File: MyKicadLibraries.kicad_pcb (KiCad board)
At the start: 2 copper layers, 184.4 x 134.7 mm, 37 parts, among them J1 Conn_01x08, J10 RCJ-22, J11 DIN-5, J12 Mini-DIN-6, J13 USB_A, J14 Conn_01x02, J15 Conn_01x02, J2 Conn_01x08, J3 POGO Pins, J4 c8-inlet, J5 FTDI, J6 Micro_SD_Card, J7 Conn_01x04, J8 Conn_02x04_Counter_Clockwise, J9 Conn_01x04, SW1 Schurter Switch, U1 radio-receiver, U10 rdm-6300, U11 magnetic-charger, U12 adafruit-MAX98357, U13 TTL, U14 lxb18, U15 esp32-wemos-d1-mini, U16 TCRT5000, U17 opb607a, U18 max98367, U19 esp-01f, U2 tp4056, U3 LilygoSIMT7000G, U4 esp-01m, U5 relais_module, U6 ESP-01, U7 dcdc, U8 mems-mic, U9 ESP-12E

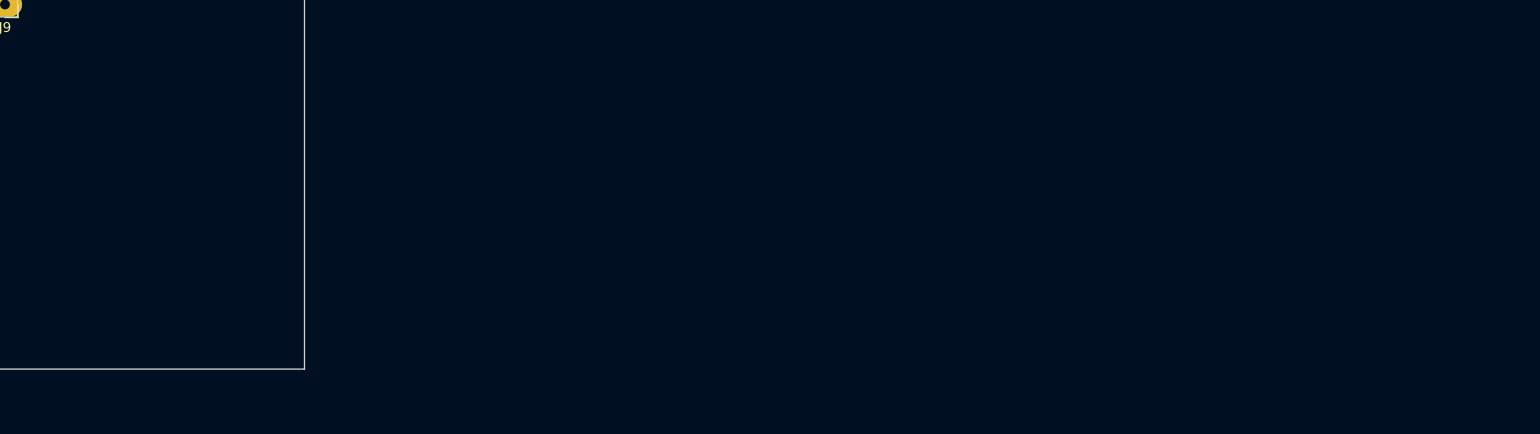
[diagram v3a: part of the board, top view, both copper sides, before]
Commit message: Add m18 bluetooth module
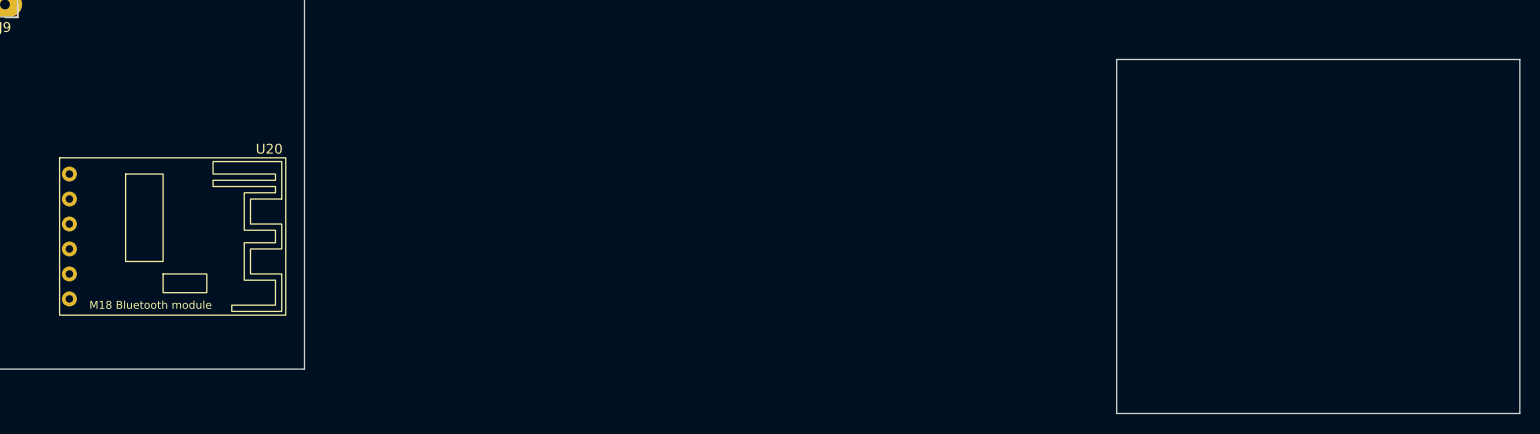
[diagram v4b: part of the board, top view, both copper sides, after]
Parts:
- added U20: m18, m18:m18, F.Cu at (228.5, 154.0)
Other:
- board size 184.4 x 134.7 mm -> 308 x 139.2 mm
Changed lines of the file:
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@@
   (net 264 "unconnected-(U19-Pad19)")
   (net 265 "unconnected-(U2-Pad6)")
+  (net 266 "unconnected-(U20-Pad1)")
+  (net 267 "unconnected-(U20-Pad2)")
+  (net 268 "unconnected-(U20-Pad3)")
+  (net 269 "unconnected-(U20-Pad4)")
+  (net 270 "unconnected-(U20-Pad5)")
+  (net 271 "unconnected-(U20-Pad6)")
   (footprint "esp-01f:esp-01f" (layer "F.Cu")
     (at 114.405 137.985)
@@
     )
   )
+  (footprint "m18:m18" (layer "F.Cu")
+    (at 228.5 154)
+    (property "Sheetfile" "MyKicadLibraries.kicad_sch")
+    (property "Sheetname" "")
+    (attr through_hole)
+    (fp_text reference "U20" (at 20.32 -8.89 unlocked) (layer "F.SilkS")
+      (effects (font (size 1 1) (thickness 0.15)))
+    )
+    (fp_text value "m18" (at 0 -8.89 unlocked) (layer "F.Fab")
+      (effects (font (size 1 1) (thickness 0.15)))
+    )
+    (fp_text user "M18 Bluetooth module" (at 8.255 6.985 unlocked) (layer "F.SilkS")
+      (effects (font (size 0.8 0.8) (thickness 0.15)))
+    )
+    (fp_text user "${REFERENCE}" (at 20.32 -8.89 unlocked) (layer "F.Fab")
+      (effects (font (size 1 1) (thickness 0.15)))
+    )
+    (fp_rect (start 5.715 -6.35) (end 9.525 2.54) (layer "F.SilkS") (width 0.12) (fill none))
+    (fp_rect (start 9.525 3.81) (end 13.97 5.715) (layer "F.SilkS") (width 0.12) (fill none))
+    (fp_rect (start -1 -8) (end 22 8) (layer "F.SilkS") (width 0.12) (fill none))
+    (fp_poly (pts
+        (xy 21.59 -3.81)
+        (xy 18.415 -3.81)
+        (xy 18.415 -1.27)
+        (xy 21.59 -1.27)
+        (xy 21.59 1.27)
+        (xy 18.415 1.27)
+        (xy 18.415 3.81)
+        (xy 21.59 3.81)
+        (xy 21.59 7.62)
+        (xy 16.51 7.62)
+        (xy 16.51 6.985)
+        (xy 20.955 6.985)
+        (xy 20.955 4.445)
+        (xy 17.78 4.445)
+        (xy 17.78 0.635)
+        (xy 20.955 0.635)
+        (xy 20.955 -0.635)
+        (xy 17.78 -0.635)
+        (xy 17.78 -4.445)
+        (xy 20.955 -4.445)
+        (xy 20.955 -5.08)
+        (xy 14.605 -5.08)
+        (xy 14.605 -5.715)
+        (xy 20.955 -5.715)
+        (xy 20.955 -6.35)
+        (xy 14.605 -6.35)
+        (xy 14.605 -7.62)
+        (xy 21.59 -7.62)
+      ) (layer "F.SilkS") (width 0.12) (fill none))
+    (pad "1" thru_hole circle (at 0 -6.35) (size 1.524 1.524) (drill 0.762) (layers *.Cu *.Mask)
+      (net 266 "unconnected-(U20-Pad1)") (pinfunction "R") (pintype "input"))
+    (pad "2" thru_hole circle (at 0 -3.81) (size 1.524 1.524) (drill 0.762) (layers *.Cu *.Mask)
+      (net 267 "unconnected-(U20-Pad2)") (pinfunction "L") (pintype "input"))
+    (pad "3" thru_hole circle (at 0 -1.27) (size 1.524 1.524) (drill 0.762) (layers *.Cu *.Mask)
+      (net 268 "unconnected-(U20-Pad3)") (pinfunction "GND") (pintype "power_in"))
+    (pad "4" thru_hole circle (at 0 1.27) (size 1.524 1.524) (drill 0.762) (layers *.Cu *.Mask)
+      (net 269 "unconnected-(U20-Pad4)") (pinfunction "VCC") (pintype "power_in"))
+    (pad "5" thru_hole circle (at 0 3.81) (size 1.524 1.524) (drill 0.762) (layers *.Cu *.Mask)
+      (net 270 "unconnected-(U20-Pad5)") (pinfunction "MUTE") (pintype "input"))
+    (pad "6" thru_hole circle (at 0 6.35) (size 1.524 1.524) (drill 0.762) (layers *.Cu *.Mask)
+      (net 271 "unconnected-(U20-Pad6)") (pinfunction "KEY") (pintype "input"))
+    (model "${KIPRJMOD}/lib/m18/m18.step"
+      (offset (xyz 13.9 -16.3 -9.3))
+      (scale (xyz 1 1 1))
+      (rotate (xyz -90 0 -180))
+    )
+  )
   (footprint "neopixel-strip:neopixel-strip" (layer "F.Cu")
     (at 72.593 100.941 90)
@@
   (gr_rect (start 206.705 143.105) (end 219.405 150.725) (layer "Edge.Cuts") (width 0.1) (fill none))
   (gr_rect (start 68.042948 32.770045) (end 252.405 167.485) (layer "Edge.Cuts") (width 0.1) (fill none))
+  (gr_rect (start 335 136) (end 376 172) (layer "Edge.Cuts") (width 0.1) (fill none))
   (segment (start 72.593 104.497) (end 90.881 104.497) (width 0.8) (layer "F.Cu") (net 82))
   (segment (start 72.593 97.385) (end 90.881 97.385) (width 0.8) (layer "F.Cu") (net 83))

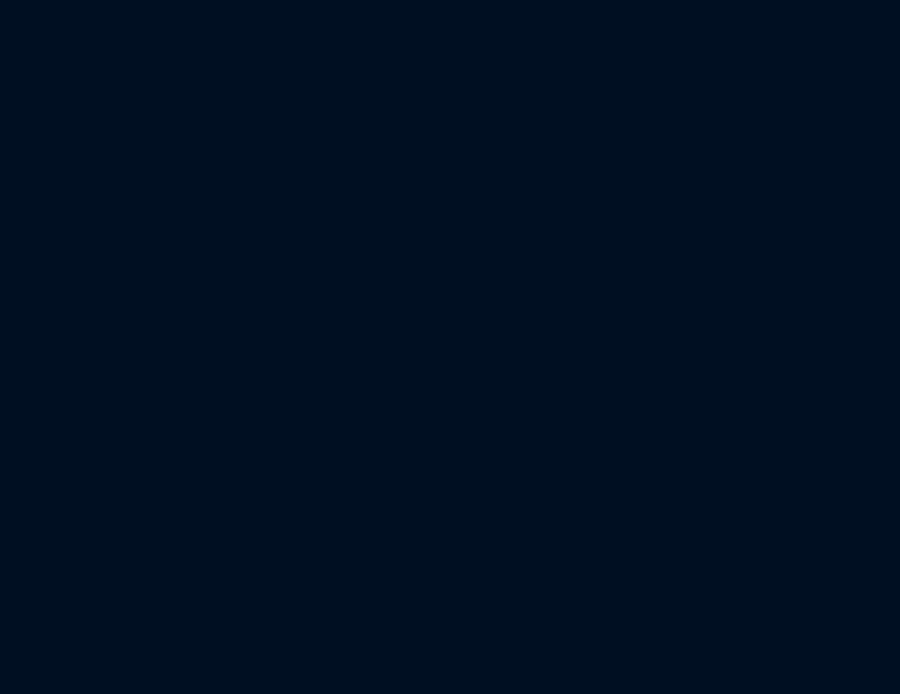
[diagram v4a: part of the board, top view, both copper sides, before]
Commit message: Add bme280 submodule
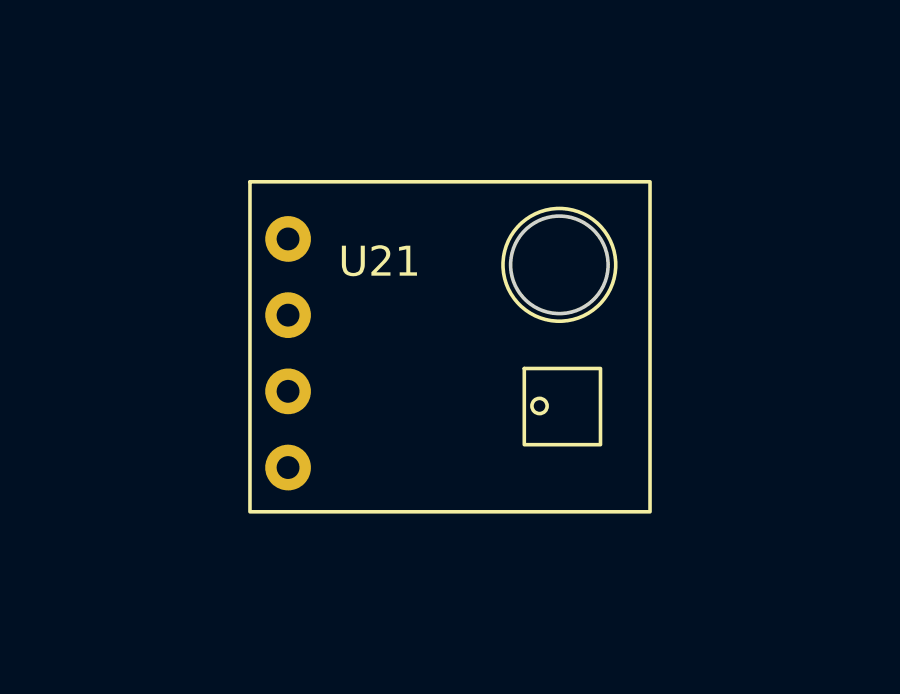
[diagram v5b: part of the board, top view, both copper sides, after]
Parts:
- added U21: bme280, bme280:bme280, F.Cu at (347.0, 154.0)
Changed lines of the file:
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@@
       (net 246 "unconnected-(U18-Pad12)") (pinfunction "SPK-") (pintype "output"))
+  )
+  (footprint "bme280:bme280" (layer "F.Cu")
+    (at 347 154)
+    (property "Sheetfile" "MyKicadLibraries.kicad_sch")
+    (property "Sheetname" "")
+    (attr through_hole)
+    (fp_text reference "U21" (at 3.048 -3.048 unlocked) (layer "F.SilkS")
+      (effects (font (size 1 1) (thickness 0.15)))
+    )
+    (fp_text value "bme280" (at 8.636 4.572 unlocked) (layer "F.Fab")
+      (effects (font (size 1 1) (thickness 0.15)))
+    )
+    (fp_text user "${REFERENCE}" (at 3.048 -4.572 unlocked) (layer "F.Fab")
+      (effects (font (size 1 1) (thickness 0.15)))
+    )
+    (fp_rect (start 7.874 0.508) (end 10.414 3.048) (layer "F.SilkS") (width 0.12) (fill none))
+    (fp_rect (start -1.27 -5.715) (end 12.065 5.285) (layer "F.SilkS") (width 0.12) (fill none))
+    (fp_circle (center 9.043 -2.947) (end 10.92218 -2.947) (layer "F.SilkS") (width 0.12) (fill none))
+    (fp_circle (center 8.381723 1.75763) (end 8.481156 1.524) (layer "F.SilkS") (width 0.12) (fill none))
+    (fp_circle (center 9.043 -2.947) (end 10.668 -2.947) (layer "Edge.Cuts") (width 0.12) (fill none))
+    (pad "1" thru_hole circle (at 0 -3.81) (size 1.524 1.524) (drill 0.762) (layers *.Cu *.Mask))
+    (pad "2" thru_hole circle (at 0 -1.27) (size 1.524 1.524) (drill 0.762) (layers *.Cu *.Mask))
+    (pad "3" thru_hole circle (at 0 1.27) (size 1.524 1.524) (drill 0.762) (layers *.Cu *.Mask))
+    (pad "4" thru_hole circle (at 0 3.81) (size 1.524 1.524) (drill 0.762) (layers *.Cu *.Mask))
+    (model "${KIPRJMOD}/lib/bme280/bme280.step"
+      (offset (xyz -1.5 0 0))
+      (scale (xyz 1 1 1))
+      (rotate (xyz 0 0 90))
+    )
   )
   (footprint "lxb18:lxb18" (layer "F.Cu")

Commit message: Update main file
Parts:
- moved U21 173.9 mm to (214.9, 40.9)
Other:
- board size 308 x 139.2 mm -> 184.4 x 134.7 mm
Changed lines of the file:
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@@
   )
   (footprint "bme280:bme280" (layer "F.Cu")
-    (at 347 154)
+    (at 214.9475 40.855)
     (property "Sheetfile" "MyKicadLibraries.kicad_sch")
     (property "Sheetname" "")
@@
   (gr_rect (start 206.705 143.105) (end 219.405 150.725) (layer "Edge.Cuts") (width 0.1) (fill none))
   (gr_rect (start 68.042948 32.770045) (end 252.405 167.485) (layer "Edge.Cuts") (width 0.1) (fill none))
-  (gr_rect (start 335 136) (end 376 172) (layer "Edge.Cuts") (width 0.1) (fill none))
   (segment (start 72.593 104.497) (end 90.881 104.497) (width 0.8) (layer "F.Cu") (net 82))
   (segment (start 72.593 97.385) (end 90.881 97.385) (width 0.8) (layer "F.Cu") (net 83))

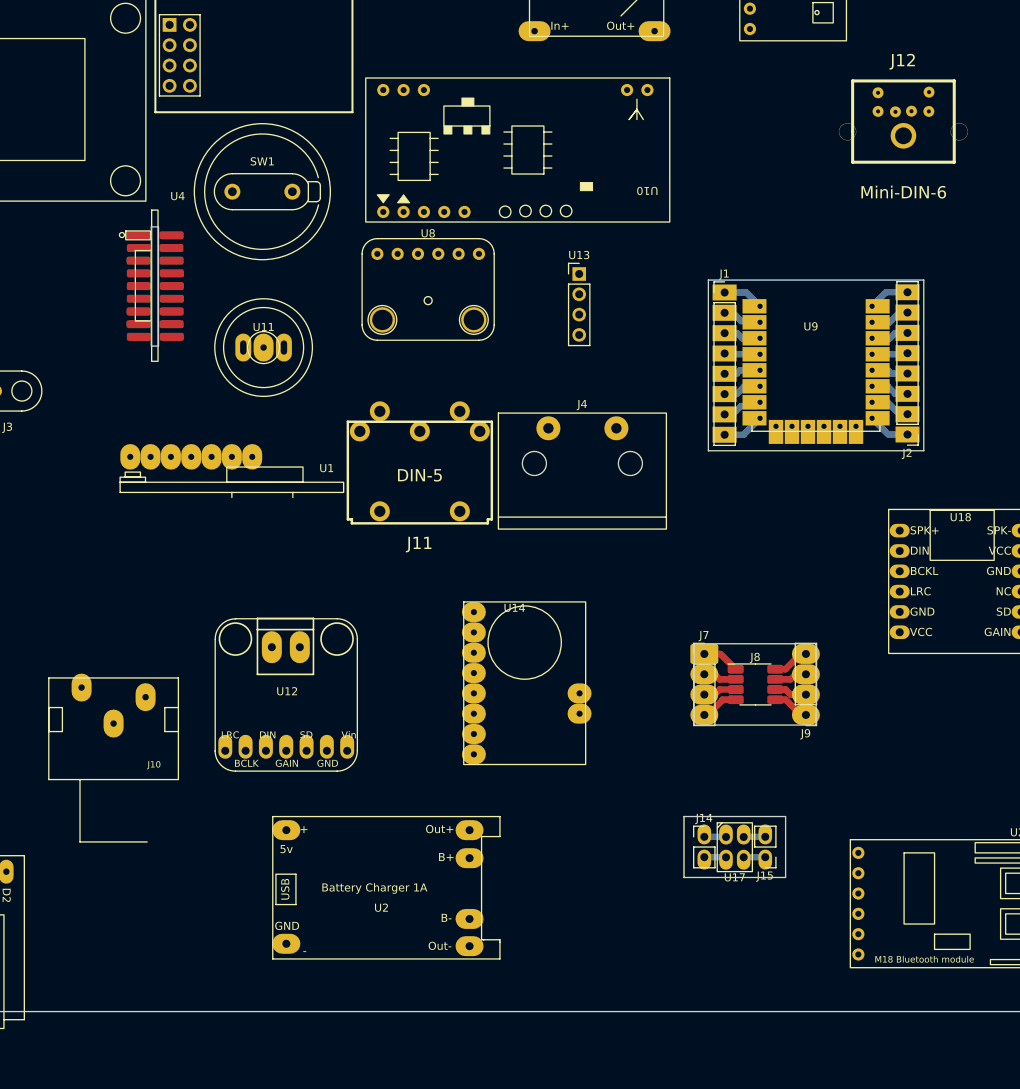
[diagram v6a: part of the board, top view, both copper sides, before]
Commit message: Add edge components to the edge
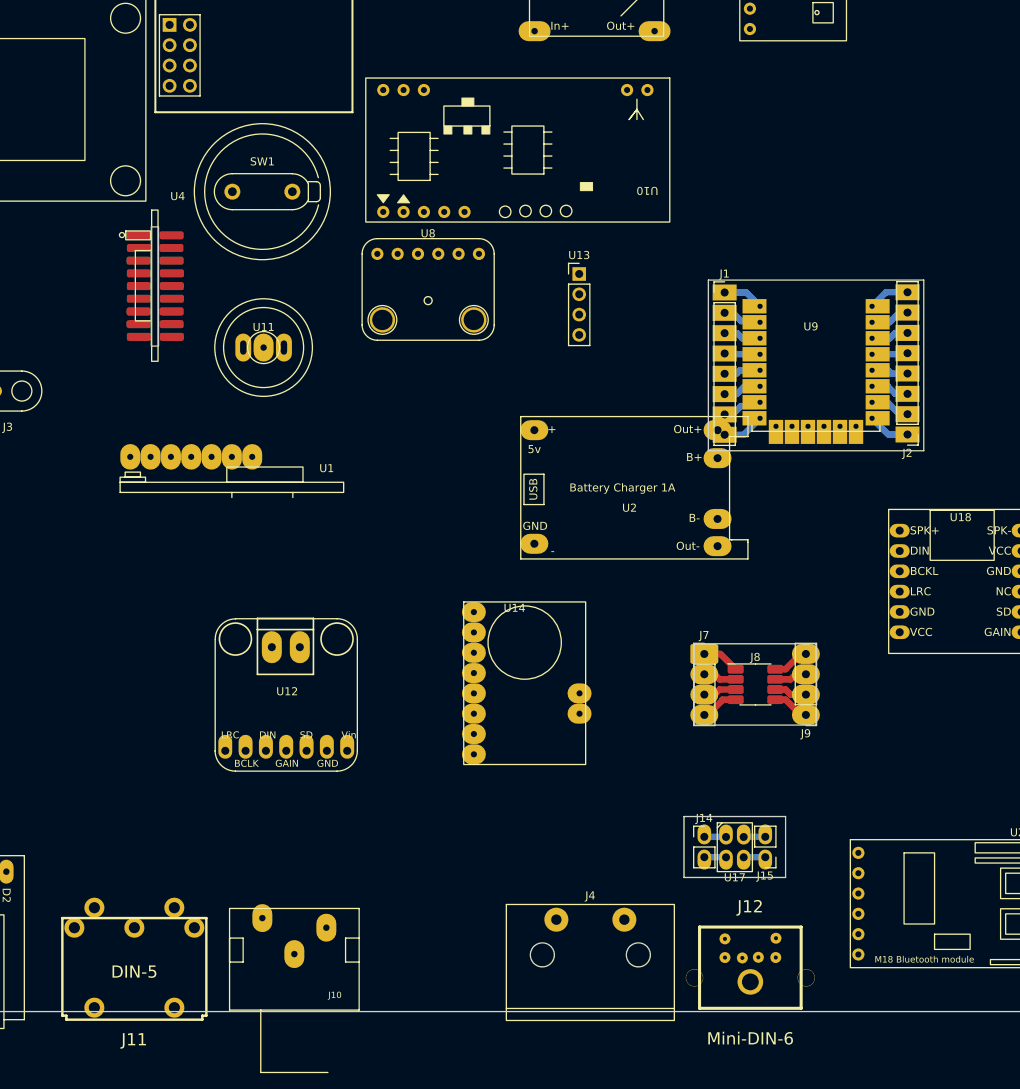
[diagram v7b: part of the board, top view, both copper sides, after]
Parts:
- moved J12 107.5 mm to (215.0, 162.0)
- moved J11 71.6 mm to (138.0, 160.0)
- moved J4 61.4 mm to (195.0, 156.0)
- moved U2 58.8 mm to (199.0, 102.0)
- moved J10 36.6 mm to (158.0, 157.3)
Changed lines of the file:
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@@
   )
   (footprint "midi:midi-din6" (layer "F.Cu")
-    (at 234.137 56.237)
+    (at 215 162)
     (tags "MINI DIN")
     (property "Sheetfile" "MyKicadLibraries.kicad_sch")
@@
   )
   (footprint "c8-inlet:c8-inlet" (layer "F.Cu")
-    (at 194.005 94.575)
+    (at 195 156)
     (descr "https://www.switchcraft.com/assets/1/24/RAPC322X_CD.PDF?4597")
     (property "Sheetfile" "MyKicadLibraries.kicad_sch")
@@
   )
   (footprint "midi:midi" (layer "F.Cu")
-    (at 173.685 97.95777)
+    (at 138 160)
     (descr "Din 5 (MIDI), Pro Signal P/N PSG03463")
     (property "Sheetfile" "MyKicadLibraries.kicad_sch")
@@
   )
   (footprint "tp4056:tp4056" (layer "F.Cu")
-    (at 168 152)
+    (at 199 102)
     (property "Sheetfile" "MyKicadLibraries.kicad_sch")
     (property "Sheetname" "")
@@
   )
   (footprint "rcj-22:rcj-22" (layer "F.Cu")
-    (at 135.405 128.485 180)
-    (property "Sheetfile" "MyKicadLibraries.kicad_sch")
-    (property "Sheetname" "")
+    (at 158 157.3 180)
+    (property "Sheetfile" "MyKicadLibraries.kicad_sch")
+    (property "Sheetname" "")

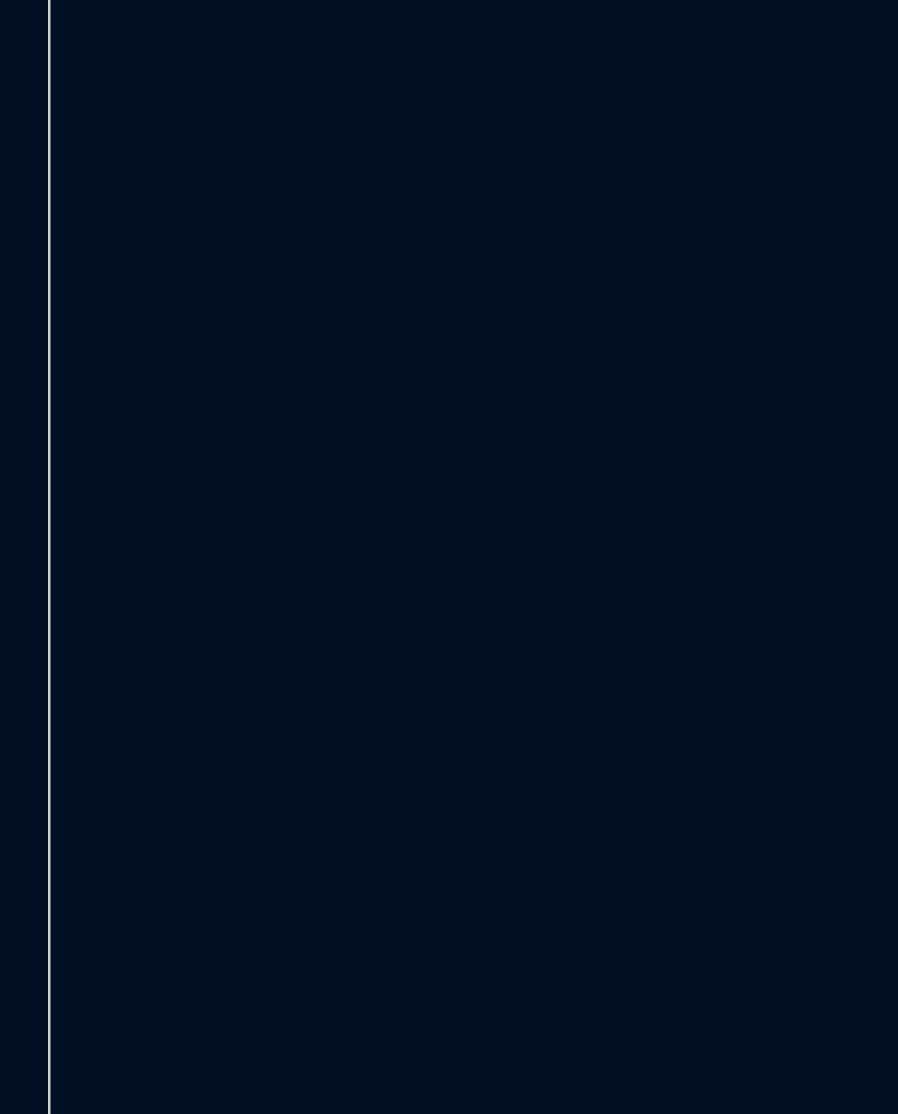
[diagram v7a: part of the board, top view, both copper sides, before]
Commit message: Add molex poe footprint
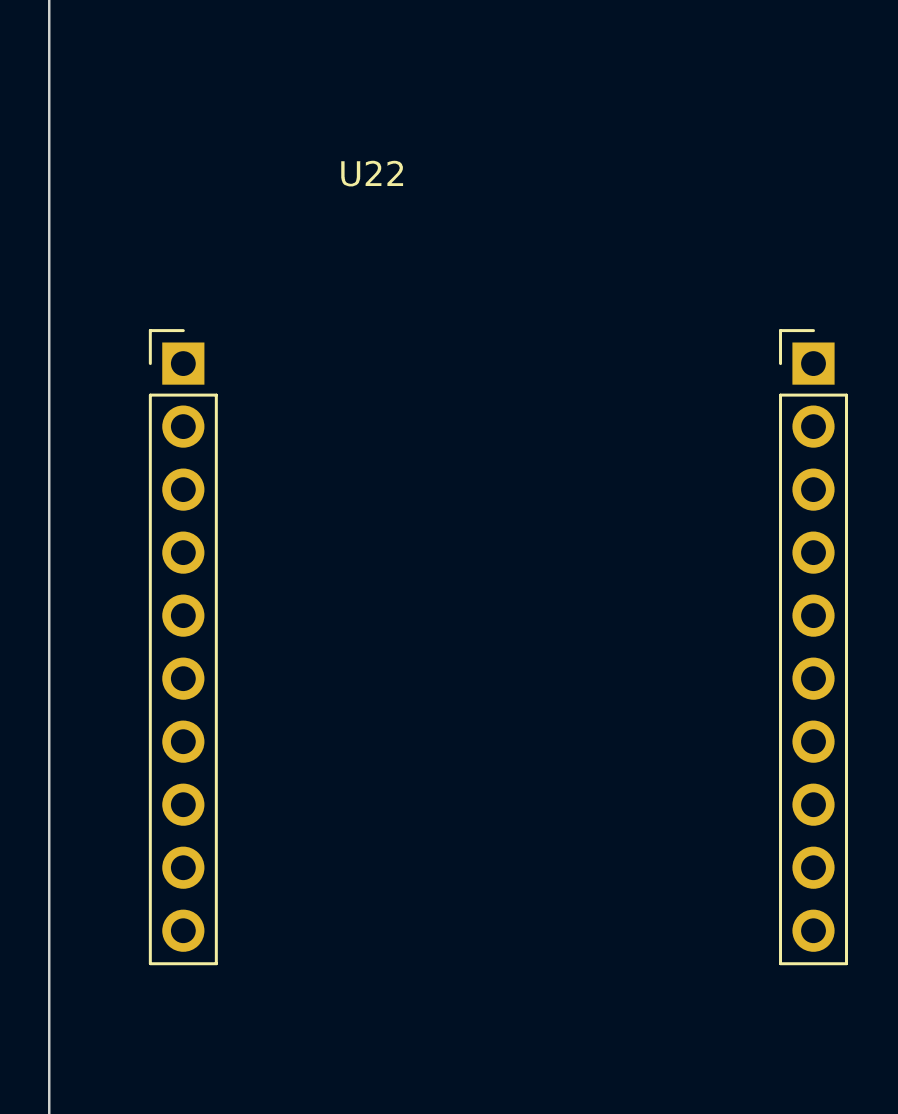
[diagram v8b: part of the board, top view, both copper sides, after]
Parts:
- added U22: ~, molex-poe:molex-poe, F.Cu at (270.5, 111.8)
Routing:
- net Net-(J1-Pin_8): track 5.28 -> 0.00 mm
- net (no net): track 0.00 -> 5.28 mm
